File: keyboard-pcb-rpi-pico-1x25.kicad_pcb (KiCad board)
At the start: 2 copper layers, 22.9 x 499.1 mm, 38 parts, among them SW1 SW_Push, SW10 SW_Push, SW11 SW_Push, SW12 SW_Push, SW13 SW_Push, SW14 SW_Push, SW15 SW_Push, SW16 SW_Push, SW17 SW_Push, SW18 SW_Push, SW19 SW_Push, SW2 SW_Push, SW20 SW_Push, SW21 SW_Push, SW22 SW_Push, SW23 SW_Push, SW24 SW_Push, SW25 SW_Push, SW3 SW_Push, SW4 SW_Push, SW5 SW_Push, SW6 SW_Push, SW7 SW_Push, SW8 SW_Push, SW9 SW_Push

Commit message: Fix width of Pico pin headers
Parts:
- SW1, SW10, SW11, SW12, SW13, SW14, SW15, SW16, SW17, SW18, SW19, SW2, SW20, SW21, SW22, SW23, SW24, SW25, SW3, SW4, SW5, SW6, SW7, SW8, SW9: footprint library:SW_Cherry_MX_1.00u_PCB -> Button_Switch_Keyboard:SW_Cherry_MX_1.00u_PCB
- moved PICO-L1 1.27 mm to (64.8, 41.9)
- moved PICO-R1 1.27 mm to (47.0, 41.9)
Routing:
- net GND: track 50.6 -> 38.6 mm, vias 3 -> 0
- net GP3: track 230.7 -> 231.9 mm
- net GP26: track 459.2 -> 460.5 mm
- net GP20: track 398.2 -> 399.5 mm
- net GP19: track 302.1 -> 303.3 mm
- net GP7: track 133.5 -> 134.8 mm
- net GP4: track 209.8 -> 211.1 mm
- net GP8: track 111.8 -> 113.0 mm
- net GP2: track 49.5 -> 50.8 mm
- net GP11: track 33.1 -> 34.4 mm
- net GP10: track 56.6 -> 57.8 mm
- net GP1: track 33.4 -> 34.7 mm
- net GP0: track 17.8 -> 19.0 mm
- net GP6: track 159.7 -> 161.0 mm
- net GP27: track 484.3 -> 485.5 mm
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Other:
- board size 22.9 x 499.1 mm -> 25.4 x 499.1 mm
- board text added: "urn:oid:1.3.6.1.4.1.39777.1.3.2.1.1"
- board text removed: "urn:oid:1.3.6.1.4.1.39777.1.3.2.1.0"

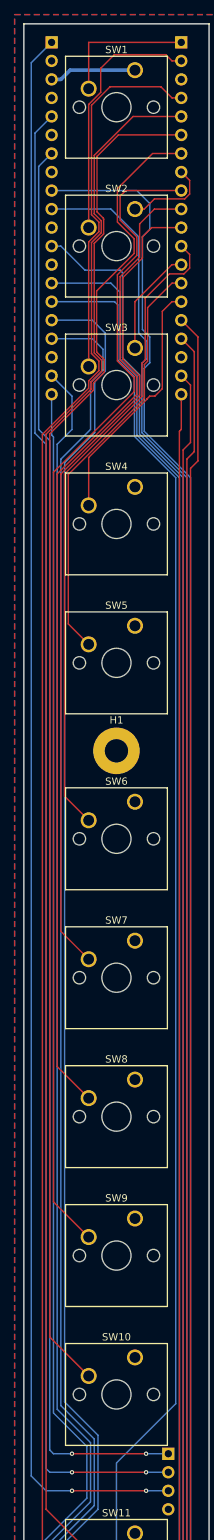
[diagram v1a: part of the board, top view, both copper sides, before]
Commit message: Increase thickness of power traces
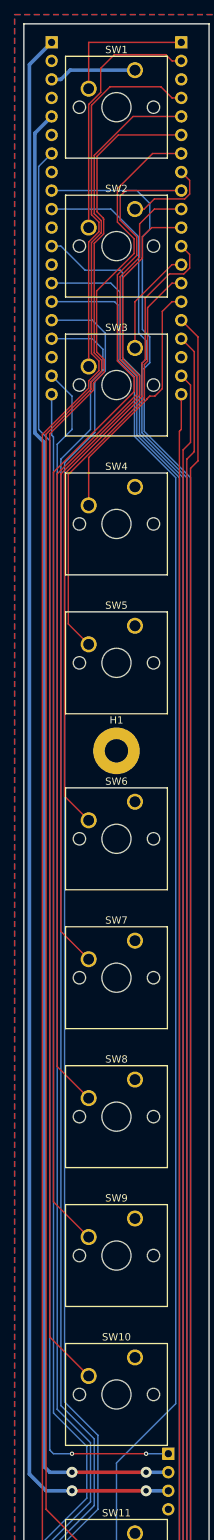
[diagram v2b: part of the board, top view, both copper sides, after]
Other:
- board text added: "urn:oid:1.3.6.1.4.1.39777.1.3.2.1.2"
- board text removed: "urn:oid:1.3.6.1.4.1.39777.1.3.2.1.1"
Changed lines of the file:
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@@
 		)
 	)
-	(gr_text "urn:oid:1.3.6.1.4.1.39777.1.3.2.1.1"
+	(gr_text "urn:oid:1.3.6.1.4.1.39777.1.3.2.1.2"
 		(at 46.99 490.22 270)
 		(layer "B.SilkS")
@@
 		(layer "Cmts.User")
 		(pts
-			(xy 52.832 235.077) (xy 43.18 235.204)
-		)
-		(height -8.128)
-		(gr_text "9.6528 mm"
-			(at 48.098466 242.167891 0.7538483331)
+			(xy 52.892 235.078) (xy 43.18 235.077)
+		)
+		(height -8.359404)
+		(gr_text "9.7120 mm"
+			(at 48.035252 242.336904 -0.005899483043)
 			(layer "Cmts.User")
 			(effects
@@
 		(start 49.784 240.538)
 		(end 59.944 240.538)
-		(width 0.2)
+		(width 0.5)
 		(layer "F.Cu")
 		(net 28)
@@
 	(via
 		(at 49.784 240.538)
-		(size 0.6)
-		(drill 0.3)
+		(size 1.5)
+		(drill 0.75)
 		(layers "F.Cu" "B.Cu")
 		(net 28)
@@
 	(via
 		(at 59.944 240.538)
-		(size 0.6)
-		(drill 0.3)
+		(size 1.5)
+		(drill 0.75)
 		(layers "F.Cu" "B.Cu")
 		(net 28)
 	)
 	(segment
+		(start 46.228 240.538)
+		(end 49.784 240.538)
+		(width 0.5)
+		(layer "B.Cu")
+		(net 28)
+	)
+	(segment
 		(start 46.99 41.91)
-		(end 44.196 44.704)
-		(width 0.2)
+		(end 43.942 44.958)
+		(width 0.5)
 		(layer "B.Cu")
 		(net 28)
@@
 		(start 62.992 240.538)
 		(end 59.944 240.538)
-		(width 0.2)
+		(width 0.5)
 		(layer "B.Cu")
 		(net 28)
 	)
 	(segment
-		(start 44.196 238.506)
+		(start 43.942 238.252)
 		(end 46.228 240.538)
-		(width 0.2)
+		(width 0.5)
 		(layer "B.Cu")
 		(net 28)
 	)
 	(segment
-		(start 46.228 240.538)
-		(end 49.784 240.538)
-		(width 0.2)
-		(layer "B.Cu")
-		(net 28)
-	)
-	(segment
-		(start 44.196 44.704)
-		(end 44.196 238.506)
-		(width 0.2)
+		(start 43.942 44.958)
+		(end 43.942 238.252)
+		(width 0.5)
 		(layer "B.Cu")
 		(net 28)
@@
 		(start 59.944 237.998)
 		(end 49.784 237.998)
-		(width 0.2)
+		(width 0.5)
 		(layer "F.Cu")
 		(net 29)
@@
 	(via
 		(at 59.944 237.998)
-		(size 0.6)
-		(drill 0.3)
+		(size 1.5)
+		(drill 0.75)
 		(layers "F.Cu" "B.Cu")
 		(net 29)
@@
 	(via
 		(at 49.784 237.998)
-		(size 0.6)
-		(drill 0.3)
+		(size 1.5)
+		(drill 0.75)
 		(layers "F.Cu" "B.Cu")
 		(net 29)
 	)
 	(segment
-		(start 46.736 237.998)
-		(end 46.228 237.49)
-		(width 0.2)
+		(start 45.974 237.236)
+		(end 45.974 96.774)
+		(width 0.5)
+		(layer "B.Cu")
+		(net 29)
+	)
+	(segment
+		(start 44.696 95.496)
+		(end 44.696 54.364)
+		(width 0.5)
 		(layer "B.Cu")
 		(net 29)
@@
 		(start 49.784 237.998)
 		(end 46.736 237.998)
-		(width 0.2)
+		(width 0.5)
 		(layer "B.Cu")
 		(net 29)
 	)
 	(segment
-		(start 46.228 237.49)
-		(end 46.228 97.028)
-		(width 0.2)
+		(start 44.696 54.364)
+		(end 46.99 52.07)
+		(width 0.5)
 		(layer "B.Cu")
 		(net 29)
 	)
 	(segment
-		(start 44.704 54.356)
-		(end 46.99 52.07)
-		(width 0.2)
+		(start 46.736 237.998)
+		(end 45.974 237.236)
+		(width 0.5)
 		(layer "B.Cu")
 		(net 29)
 	)
 	(segment
-		(start 46.228 97.028)
-		(end 44.704 95.504)
-		(width 0.2)
-		(layer "B.Cu")
-		(net 29)
-	)
-	(segment
-		(start 44.704 95.504)
-		(end 44.704 54.356)
-		(width 0.2)
+		(start 45.974 96.774)
+		(end 44.696 95.496)
+		(width 0.5)
 		(layer "B.Cu")
 		(net 29)
@@
 		(start 62.992 237.998)
 		(end 59.944 237.998)
-		(width 0.2)
+		(width 0.5)
 		(layer "B.Cu")
 		(net 29)

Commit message: Add Area X quote
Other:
- board text added: "The shadows of the abyss are like the petals of a monstrous flower that shall blossom within the skull and expand the mind beyond what any man can bear, but whether it decays under the earth or above on green fields, or out to sea or in the very air, all shall come to revelation, and to revel, in the knowledge of the strangling fruit and the hand of the sinner shall rejoice, for there is no sin i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"
- board text added: "Where lies the strangling fruit that came from the hand of the sinner I shall bring forth the seeds of the dead to share with the worms that gather in the darkness and surround the world with the power of their lives while from the dim-lit halls of other places forms that never could be writhe for the impatience of the few who have never seen or been seen. In the black water with the sun shining 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"
- board text added: "and their teeth shall devour and sustain and herald the passing of an age. That which dies shall still know life in death for all that decays is not forgotten and reanimated shall walk the world in the bliss of not-knowing. There shall be a fire that knows your name, and in the presence of the strangling fruit, its dark flame shall acquire every part of you. -- Jeff VanderMeer, Annihilation (2014)"
- board text added: "urn:oid:1.3.6.1.4.1.39777.1.3.2.1.3"
- board text removed: "urn:oid:1.3.6.1.4.1.39777.1.3.2.1.2"
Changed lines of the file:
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@@
 		)
 	)
-	(gr_text "urn:oid:1.3.6.1.4.1.39777.1.3.2.1.2"
+	(gr_text "urn:oid:1.3.6.1.4.1.39777.1.3.2.1.3"
 		(at 46.99 490.22 270)
 		(layer "B.SilkS")
@@
 		)
 	)
+	(gr_text " and their teeth shall devour and sustain and herald the passing of an age.  That which dies shall still know life in death for all that decays is not forgotten and reanimated shall walk the world in the bliss of not-knowing.  There shall be a fire that knows your name, and in the presence of the strangling fruit, its dark flame shall acquire every part of you.  -- Jeff VanderMeer, Annihilation (2014)"
+		(at 66.802 537.591 270)
+		(layer "B.SilkS")
+		(effects
+			(font
+				(size 1 1)
+				(thickness 0.2)
+				(bold yes)
+			)
+			(justify left mirror)
+		)
+	)
 	(gr_text "https://github.com/nomis/keyboard-pcb-rpi-pico-1x25"
 		(at 46.99 389.89 270)
@@
 		)
 	)
+	(gr_text "The shadows of the abyss are like the petals of a monstrous flower that shall blossom within the skull and expand the mind beyond what any man can bear, but whether it decays under the earth or above on green fields, or out to sea or in the very air, all shall come to revelation, and to revel, in the knowledge of the strangling fruit and the hand of the sinner shall rejoice, for there is no sin in shadow or in light that the seeds of the dead cannot forgive.  There shall be in the planting in the shadows a grace and a mercy that shall bloom dark flowers,"
+		(at 66.802 98.044 270)
+		(layer "F.SilkS")
+		(effects
+			(font
+				(size 1 1)
+				(thickness 0.2)
+				(bold yes)
+			)
+			(justify left)
+		)
+	)
+	(gr_text "Where lies the strangling fruit that came from the hand of the sinner I shall bring forth the seeds of the dead to share with the worms that gather in the darkness and surround the world with the power of their lives while from the dim-lit halls of other places forms that never could be writhe for the impatience of the few who have never seen or been seen.  In the black water with the sun shining at midnight, those fruit shall come ripe and in the darkness of that which is golden shall split open to reveal the revelation of the fatal softness in the earth."
+		(at 44.958 536.829 90)
+		(layer "F.SilkS")
+		(effects
+			(font
+				(size 1 1)
+				(thickness 0.2)
+				(bold yes)
+			)
+			(justify left)
+		)
+	)

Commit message: Change routing to improve ground planes
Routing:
- net GND: track 38.6 -> 0.00 mm
- net GP27: track 485.5 -> 499.0 mm
- net GP2: track 50.8 -> 43.0 mm
- net GP6: track 161.0 -> 157.2 mm
- net GP3: track 231.9 -> 228.2 mm
- net GP4: track 211.1 -> 207.3 mm
- net GP5: track 182.4 -> 184.4 mm
- net GP20: track 399.5 -> 397.7 mm
- net GP8: track 113.0 -> 114.6 mm
- net GP26: track 460.5 -> 462.0 mm
- net GP21: track 410.9 -> 409.4 mm
- net GP1: track 34.7 -> 36.0 mm
- net GP22: track 434.2 -> 435.4 mm
- net GP7: track 134.8 -> 135.8 mm

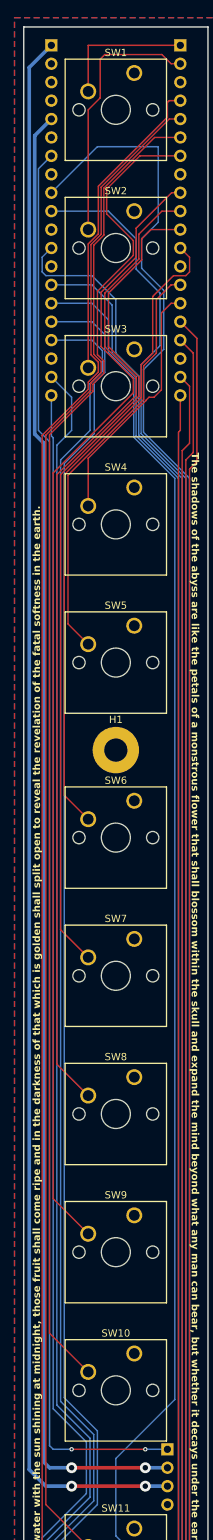
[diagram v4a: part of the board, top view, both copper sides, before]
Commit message: Move vias so that they're not directly under silkscreen
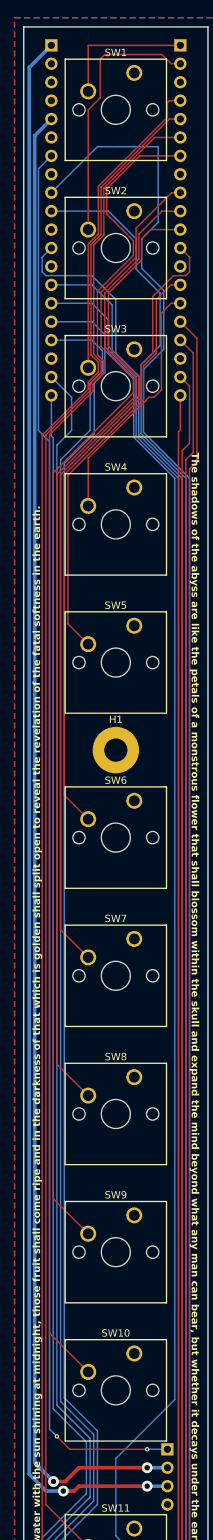
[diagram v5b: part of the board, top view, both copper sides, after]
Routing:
- net +3.3V: track 204.0 -> 206.3 mm
- net GP28: track 195.6 -> 194.3 mm
- net +5V: track 217.6 -> 218.6 mm
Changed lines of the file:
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@@
 	)
 	(segment
-		(start 49.784 235.458)
-		(end 59.944 235.458)
-		(width 0.2)
-		(layer "F.Cu")
-		(net 27)
-	)
-	(via
-		(at 49.784 235.458)
+		(start 60.198 235.458)
+		(end 49.53 235.458)
+		(width 0.2)
+		(layer "F.Cu")
+		(net 27)
+	)
+	(segment
+		(start 49.53 235.458)
+		(end 47.752 233.68)
+		(width 0.2)
+		(layer "F.Cu")
+		(net 27)
+	)
+	(via
+		(at 47.752 233.68)
 		(size 0.6)
 		(drill 0.3)
@@
 	)
 	(via
-		(at 59.944 235.458)
+		(at 60.198 235.458)
 		(size 0.6)
 		(drill 0.3)
@@
 	)
 	(segment
-		(start 47.244 235.458)
-		(end 46.736 234.95)
-		(width 0.2)
-		(layer "B.Cu")
-		(net 27)
-	)
-	(segment
-		(start 59.944 235.458)
+		(start 46.736 96.52)
+		(end 45.212 94.996)
+		(width 0.2)
+		(layer "B.Cu")
+		(net 27)
+	)
+	(segment
+		(start 60.198 235.458)
 		(end 62.992 235.458)
 		(width 0.2)
@@
 	)
 	(segment
-		(start 46.736 234.95)
+		(start 45.212 94.996)
+		(end 45.212 58.928)
+		(width 0.2)
+		(layer "B.Cu")
+		(net 27)
+	)
+	(segment
+		(start 46.736 232.664)
 		(end 46.736 96.52)
+		(width 0.2)
+		(layer "B.Cu")
+		(net 27)
+	)
+	(segment
+		(start 47.752 233.68)
+		(end 46.736 232.664)
 		(width 0.2)
 		(layer "B.Cu")
@@
 	)
 	(segment
-		(start 49.784 235.458)
-		(end 47.244 235.458)
-		(width 0.2)
-		(layer "B.Cu")
-		(net 27)
-	)
-	(segment
-		(start 46.736 96.52)
-		(end 45.212 94.996)
-		(width 0.2)
-		(layer "B.Cu")
-		(net 27)
-	)
-	(segment
-		(start 45.212 94.996)
-		(end 45.212 58.928)
-		(width 0.2)
-		(layer "B.Cu")
-		(net 27)
-	)
-	(segment
-		(start 49.784 240.538)
+		(start 50.12761 241.21039)
+		(end 50.8 240.538)
+		(width 0.5)
+		(layer "F.Cu")
+		(net 28)
+	)
+	(segment
+		(start 50.8 240.538)
 		(end 59.944 240.538)
 		(width 0.5)
@@
 		(net 28)
 	)
-	(via
-		(at 49.784 240.538)
-		(size 1.5)
-		(drill 0.75)
-		(layers "F.Cu" "B.Cu")
-		(net 28)
-	)
-	(via
-		(at 59.944 240.538)
-		(size 1.5)
-		(drill 0.75)
-		(layers "F.Cu" "B.Cu")
-		(net 28)
-	)
-	(segment
-		(start 46.228 240.538)
-		(end 49.784 240.538)
-		(width 0.5)
-		(layer "B.Cu")
-		(net 28)
-	)
-	(segment
-		(start 46.99 41.91)
-		(end 43.942 44.958)
+	(segment
+		(start 48.43982 241.166237)
+		(end 48.43982 241.21039)
+		(width 0.5)
+		(layer "F.Cu")
+		(net 28)
+	)
+	(segment
+		(start 48.43982 241.21039)
+		(end 50.12761 241.21039)
+		(width 0.5)
+		(layer "F.Cu")
+		(net 28)
+	)
+	(via
+		(at 48.641 241.21039)
+		(size 1.5)
+		(drill 0.75)
+		(layers "F.Cu" "B.Cu")
+		(net 28)
+	)
+	(via
+		(at 60.198 240.538)
+		(size 1.5)
+		(drill 0.75)
+		(layers "F.Cu" "B.Cu")
+		(net 28)
+	)
+	(segment
+		(start 48.43982 241.21039)
+		(end 46.26539 241.21039)
 		(width 0.5)
 		(layer "B.Cu")
@@
 	)
 	(segment
-		(start 43.942 238.252)
-		(end 46.228 240.538)
+		(start 46.26539 241.21039)
+		(end 43.942 238.887)
 		(width 0.5)
 		(layer "B.Cu")
@@
 	(segment
 		(start 43.942 44.958)
-		(end 43.942 238.252)
-		(width 0.5)
-		(layer "B.Cu")
-		(net 28)
-	)
-	(segment
-		(start 59.944 237.998)
-		(end 49.784 237.998)
-		(width 0.5)
-		(layer "F.Cu")
-		(net 29)
-	)
-	(via
-		(at 59.944 237.998)
-		(size 1.5)
-		(drill 0.75)
-		(layers "F.Cu" "B.Cu")
-		(net 29)
-	)
-	(via
-		(at 49.784 237.998)
-		(size 1.5)
-		(drill 0.75)
-		(layers "F.Cu" "B.Cu")
-		(net 29)
-	)
-	(segment
-		(start 45.974 237.236)
-		(end 45.974 96.774)
-		(width 0.5)
-		(layer "B.Cu")
-		(net 29)
-	)
-	(segment
-		(start 44.696 95.496)
-		(end 44.696 54.364)
-		(width 0.5)
-		(layer "B.Cu")
-		(net 29)
-	)
-	(segment
-		(start 49.784 237.998)
-		(end 46.736 237.998)
-		(width 0.5)
-		(layer "B.Cu")
+		(end 46.99 41.91)
+		(width 0.5)
+		(layer "B.Cu")
+		(net 28)
+	)
+	(segment
+		(start 43.942 238.887)
+		(end 43.942 44.958)
+		(width 0.5)
+		(layer "B.Cu")
+		(net 28)
+	)
+	(segment
+		(start 60.198 237.998)
+		(end 50.8 237.998)
+		(width 0.5)
+		(layer "F.Cu")
+		(net 29)
+	)
+	(segment
+		(start 50.8 237.998)
+		(end 48.901029 239.896971)
+		(width 0.5)
+		(layer "F.Cu")
+		(net 29)
+	)
+	(segment
+		(start 48.901029 239.896971)
+		(end 47.284029 239.896971)
+		(width 0.5)
+		(layer "F.Cu")
+		(net 29)
+	)
+	(via
+		(at 60.198 237.998)
+		(size 1.5)
+		(drill 0.75)
+		(layers "F.Cu" "B.Cu")
+		(net 29)
+	)
+	(via
+		(at 47.284029 239.896971)
+		(size 1.5)
+		(drill 0.75)
+		(layers "F.Cu" "B.Cu")
 		(net 29)
 	)
@@
 	)
 	(segment
-		(start 46.736 237.998)
-		(end 45.974 237.236)
-		(width 0.5)
-		(layer "B.Cu")
-		(net 29)
-	)
-	(segment
-		(start 45.974 96.774)
-		(end 44.696 95.496)
+		(start 44.696 237.308942)
+		(end 44.696 54.364)
+		(width 0.5)
+		(layer "B.Cu")
+		(net 29)
+	)
+	(segment
+		(start 47.284029 239.896971)
+		(end 44.696 237.308942)
 		(width 0.5)
 		(layer "B.Cu")
@@
 	(segment
 		(start 62.992 237.998)
-		(end 59.944 237.998)
-		(width 0.5)
-		(layer "B.Cu")
+		(end 60.198 237.998)
+		(width 0.5)
+		(layer "B.Cu")
